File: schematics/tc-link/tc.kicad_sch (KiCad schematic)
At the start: 7 parts, among them U1 MAX31856

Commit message: Nearly completly schematics
Signed-off-by: Andrew Balmos <abalmos@purdue.edu>
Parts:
- renumbered C1 to C4, C3 to C5, C4 to C6, C5 to C7, R1 to R3, R2 to R4, U1 to U2
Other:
- moved on the sheet: C7
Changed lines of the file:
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@@
 	(wire
 		(pts
-			(xy 170.18 123.19) (xy 170.18 125.73)
+			(xy 218.44 72.39) (xy 218.44 74.93)
 		)
 		(stroke
@@
 	(wire
 		(pts
-			(xy 170.18 130.81) (xy 170.18 133.35)
+			(xy 218.44 80.01) (xy 218.44 82.55)
 		)
 		(stroke
@@
 	(symbol
 		(lib_id "power:+3V3")
-		(at 170.18 123.19 0)
+		(at 218.44 72.39 0)
 		(unit 1)
 		(exclude_from_sim no)
@@
 		(dnp no)
 		(fields_autoplaced yes)
-		(property "Reference" "#PWR013"
-			(at 170.18 127 0)
+		(property "Reference" "#PWR040"
+			(at 218.44 76.2 0)
 			(effects
 				(font
@@
 		)
 		(property "Value" "+3V3"
-			(at 170.18 118.11 0)
+			(at 218.44 67.31 0)
 			(effects
 				(font
@@
 		)
 		(property "Footprint" ""
-			(at 170.18 123.19 0)
+			(at 218.44 72.39 0)
 			(effects
 				(font
@@
 		)
 		(property "Datasheet" ""
-			(at 170.18 123.19 0)
+			(at 218.44 72.39 0)
 			(effects
 				(font
@@
 		)
 		(property "Description" "Power symbol creates a global label with name \"+3V3\""
-			(at 170.18 123.19 0)
+			(at 218.44 72.39 0)
 			(effects
 				(font
@@
 			(project "tc-link"
 				(path "/8e86abba-54e7-4e79-af31-15eabcc8dc53/cf0945b2-2b77-4b7a-9180-f6abb82eccbe"
-					(reference "#PWR010")
+					(reference "#PWR046")
 					(unit 1)
 				)
 				(path "/8e86abba-54e7-4e79-af31-15eabcc8dc53/d82a3210-8cdf-44cf-8f3c-363268ea9818"
-					(reference "#PWR013")
+					(reference "#PWR040")
 					(unit 1)
 				)
@@
 	(symbol
 		(lib_id "power:GND")
-		(at 170.18 133.35 0)
+		(at 218.44 82.55 0)
 		(unit 1)
 		(exclude_from_sim no)
@@
 		(dnp no)
 		(fields_autoplaced yes)
-		(property "Reference" "#PWR014"
-			(at 170.18 139.7 0)
+		(property "Reference" "#PWR041"
+			(at 218.44 88.9 0)
 			(effects
 				(font
@@
 		)
 		(property "Value" "GND"
-			(at 170.18 138.43 0)
+			(at 218.44 87.63 0)
 			(effects
 				(font
@@
 		)
 		(property "Footprint" ""
-			(at 170.18 133.35 0)
+			(at 218.44 82.55 0)
 			(effects
 				(font
@@
 		)
 		(property "Datasheet" ""
-			(at 170.18 133.35 0)
+			(at 218.44 82.55 0)
 			(effects
 				(font
@@
 		)
 		(property "Description" "Power symbol creates a global label with name \"GND\" , ground"
-			(at 170.18 133.35 0)
+			(at 218.44 82.55 0)
 			(effects
 				(font
@@
 			(project "tc-link"
 				(path "/8e86abba-54e7-4e79-af31-15eabcc8dc53/cf0945b2-2b77-4b7a-9180-f6abb82eccbe"
-					(reference "#PWR012")
+					(reference "#PWR047")
 					(unit 1)
 				)
 				(path "/8e86abba-54e7-4e79-af31-15eabcc8dc53/d82a3210-8cdf-44cf-8f3c-363268ea9818"
-					(reference "#PWR014")
+					(reference "#PWR041")
 					(unit 1)
 				)
@@
 		(dnp no)
 		(fields_autoplaced yes)
-		(property "Reference" "C3"
+		(property "Reference" "C5"
 			(at 134.62 76.1935 0)
 			(effects
@@
 			(project "tc-link"
 				(path "/8e86abba-54e7-4e79-af31-15eabcc8dc53/cf0945b2-2b77-4b7a-9180-f6abb82eccbe"
-					(reference "C12")
+					(reference "C9")
 					(unit 1)
 				)
 				(path "/8e86abba-54e7-4e79-af31-15eabcc8dc53/d82a3210-8cdf-44cf-8f3c-363268ea9818"
-					(reference "C3")
+					(reference "C5")
 					(unit 1)
 				)
@@
 		(dnp no)
 		(fields_autoplaced yes)
-		(property "Reference" "R1"
+		(property "Reference" "R3"
 			(at 123.19 66.04 90)
 			(effects
@@
 			(project "tc-link"
 				(path "/8e86abba-54e7-4e79-af31-15eabcc8dc53/cf0945b2-2b77-4b7a-9180-f6abb82eccbe"
-					(reference "R1")
+					(reference "R5")
 					(unit 1)
 				)
 				(path "/8e86abba-54e7-4e79-af31-15eabcc8dc53/d82a3210-8cdf-44cf-8f3c-363268ea9818"
-					(reference "R1")
+					(reference "R3")
 					(unit 1)
 				)
@@
 		(dnp no)
 		(fields_autoplaced yes)
-		(property "Reference" "C4"
+		(property "Reference" "C6"
 			(at 134.62 86.3535 0)
 			(effects
@@
 			(project "tc-link"
 				(path "/8e86abba-54e7-4e79-af31-15eabcc8dc53/cf0945b2-2b77-4b7a-9180-f6abb82eccbe"
-					(reference "C16")
+					(reference "C10")
 					(unit 1)
 				)
 				(path "/8e86abba-54e7-4e79-af31-15eabcc8dc53/d82a3210-8cdf-44cf-8f3c-363268ea9818"
-					(reference "C4")
+					(reference "C6")
 					(unit 1)
 				)
@@
 		(dnp no)
 		(fields_autoplaced yes)
-		(property "Reference" "C1"
+		(property "Reference" "C4"
 			(at 134.62 64.7635 0)
 			(effects
@@
 			(project "tc-link"
 				(path "/8e86abba-54e7-4e79-af31-15eabcc8dc53/cf0945b2-2b77-4b7a-9180-f6abb82eccbe"
-					(reference "C14")
+					(reference "C8")
 					(unit 1)
 				)
 				(path "/8e86abba-54e7-4e79-af31-15eabcc8dc53/d82a3210-8cdf-44cf-8f3c-363268ea9818"
-					(reference "C1")
+					(reference "C4")
 					(unit 1)
 				)
@@
 		(dnp no)
 		(fields_autoplaced yes)
-		(property "Reference" "R2"
+		(property "Reference" "R4"
 			(at 123.19 76.2 90)
 			(effects
@@
 			(project "tc-link"
 				(path "/8e86abba-54e7-4e79-af31-15eabcc8dc53/cf0945b2-2b77-4b7a-9180-f6abb82eccbe"
-					(reference "R8")
+					(reference "R6")
 					(unit 1)
 				)
 				(path "/8e86abba-54e7-4e79-af31-15eabcc8dc53/d82a3210-8cdf-44cf-8f3c-363268ea9818"
-					(reference "R2")
+					(reference "R4")
 					(unit 1)
 				)
@@
 		(dnp no)
 		(fields_autoplaced yes)
-		(property "Reference" "#PWR05"
+		(property "Reference" "#PWR036"
 			(at 128.27 64.77 0)
 			(effects
@@
 			(project "tc-link"
 				(path "/8e86abba-54e7-4e79-af31-15eabcc8dc53/cf0945b2-2b77-4b7a-9180-f6abb82eccbe"
-					(reference "#PWR032")
+					(reference "#PWR042")
 					(unit 1)
 				)
 				(path "/8e86abba-54e7-4e79-af31-15eabcc8dc53/d82a3210-8cdf-44cf-8f3c-363268ea9818"
-					(reference "#PWR05")
+					(reference "#PWR036")
 					(unit 1)
 				)
@@
 		(dnp no)
 		(fields_autoplaced yes)
-		(property "Reference" "U1"
+		(property "Reference" "U2"
 			(at 172.3233 60.96 0)
 			(effects
@@
 			(project "tc-link"
 				(path "/8e86abba-54e7-4e79-af31-15eabcc8dc53/cf0945b2-2b77-4b7a-9180-f6abb82eccbe"
-					(reference "U1")
+					(reference "U3")
 					(unit 1)
 				)
 				(path "/8e86abba-54e7-4e79-af31-15eabcc8dc53/d82a3210-8cdf-44cf-8f3c-363268ea9818"
-					(reference "U1")
+					(reference "U2")
 					(unit 1)
 				)
@@
 	(symbol
 		(lib_id "Device:C_Small")
-		(at 170.18 128.27 0)
+		(at 218.44 77.47 0)
 		(unit 1)
 		(exclude_from_sim no)
@@
 		(dnp no)
 		(fields_autoplaced yes)
-		(property "Reference" "C5"
-			(at 172.72 127.0062 0)
+		(property "Reference" "C7"
+			(at 220.98 76.2062 0)
 			(effects
 				(font
@@
 		)
 		(property "Value" "100n"
-			(at 172.72 129.5462 0)
+			(at 220.98 78.7462 0)
 			(effects
 				(font
@@
 		)
 		(property "Footprint" ""
-			(at 170.18 128.27 0)
+			(at 218.44 77.47 0)
 			(effects
 				(font
@@
 		)
 		(property "Datasheet" "~"
-			(at 170.18 128.27 0)
+			(at 218.44 77.47 0)
 			(effects
 				(font
@@
 		)
 		(property "Description" "Unpolarized capacitor, small symbol"
-			(at 170.18 128.27 0)
+			(at 218.44 77.47 0)
 			(effects
 				(font
@@
 			(project "tc-link"
 				(path "/8e86abba-54e7-4e79-af31-15eabcc8dc53/cf0945b2-2b77-4b7a-9180-f6abb82eccbe"
-					(reference "C5")
+					(reference "C11")
 					(unit 1)
 				)
 				(path "/8e86abba-54e7-4e79-af31-15eabcc8dc53/d82a3210-8cdf-44cf-8f3c-363268ea9818"
-					(reference "C5")
+					(reference "C7")
 					(unit 1)
 				)
@@
 		(dnp no)
 		(fields_autoplaced yes)
-		(property "Reference" "#PWR07"
+		(property "Reference" "#PWR037"
 			(at 132.08 100.33 0)
 			(effects
@@
 			(project "tc-link"
 				(path "/8e86abba-54e7-4e79-af31-15eabcc8dc53/cf0945b2-2b77-4b7a-9180-f6abb82eccbe"
-					(reference "#PWR030")
+					(reference "#PWR043")
 					(unit 1)
 				)
 				(path "/8e86abba-54e7-4e79-af31-15eabcc8dc53/d82a3210-8cdf-44cf-8f3c-363268ea9818"
-					(reference "#PWR07")
+					(reference "#PWR037")
 					(unit 1)
 				)
@@
 		(dnp no)
 		(fields_autoplaced yes)
-		(property "Reference" "#PWR011"
+		(property "Reference" "#PWR039"
 			(at 167.64 104.14 0)
 			(effects
@@
 			(project "tc-link"
 				(path "/8e86abba-54e7-4e79-af31-15eabcc8dc53/cf0945b2-2b77-4b7a-9180-f6abb82eccbe"
-					(reference "#PWR06")
+					(reference "#PWR045")
 					(unit 1)
 				)
 				(path "/8e86abba-54e7-4e79-af31-15eabcc8dc53/d82a3210-8cdf-44cf-8f3c-363268ea9818"
-					(reference "#PWR011")
+					(reference "#PWR039")
 					(unit 1)
 				)
@@
 		(dnp no)
 		(fields_autoplaced yes)
-		(property "Reference" "#PWR09"
+		(property "Reference" "#PWR038"
 			(at 167.64 59.69 0)
 			(effects
@@
 			(project "tc-link"
 				(path "/8e86abba-54e7-4e79-af31-15eabcc8dc53/cf0945b2-2b77-4b7a-9180-f6abb82eccbe"
-					(reference "#PWR08")
+					(reference "#PWR044")
 					(unit 1)
 				)
 				(path "/8e86abba-54e7-4e79-af31-15eabcc8dc53/d82a3210-8cdf-44cf-8f3c-363268ea9818"
-					(reference "#PWR09")
-					(unit 1)
-				)
+					(reference "#PWR038")
+					(unit 1)
+				)

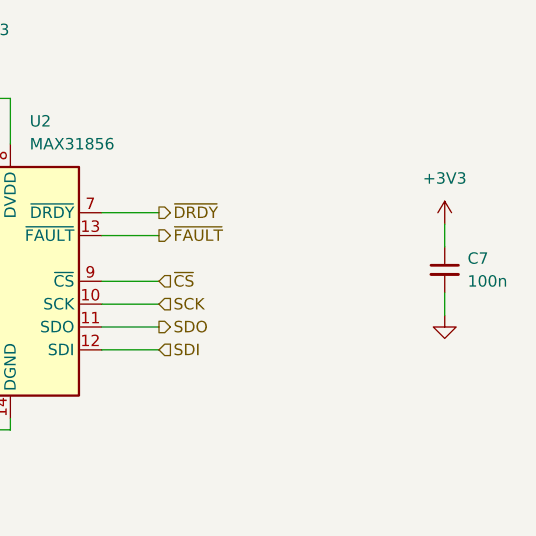
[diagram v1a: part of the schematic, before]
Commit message: release(tc-link): v1.0. Sent for production.
Signed-off-by: Andrew Balmos <abalmos@purdue.edu>
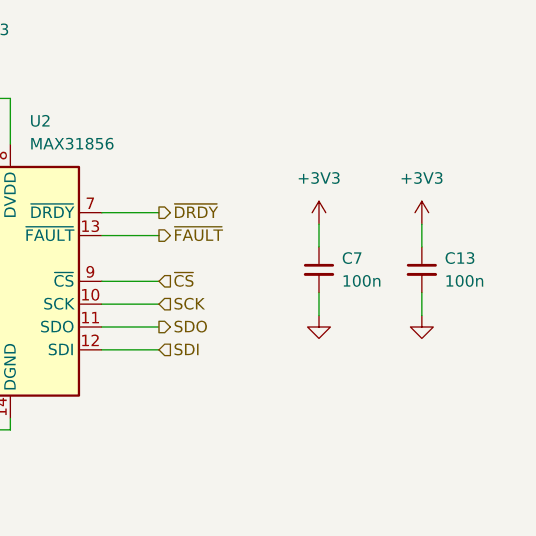
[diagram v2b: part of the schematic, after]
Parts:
- added C13: 100n, Capacitor_SMD:C_0603_1608Metric, symbol Device:C_Small
- C4, C6: footprint Capacitor_SMD:C_0402_1005Metric -> Capacitor_SMD:C_0603_1608Metric; LCSC (none) -> C327204; MPN (none) -> CC0603KRX7R8BB103
- C5: footprint Capacitor_SMD:C_0402_1005Metric -> Capacitor_SMD:C_0603_1608Metric; LCSC (none) -> C6119867; MPN (none) -> CGA0603X7R104K500JT
- C7: footprint (none) -> Capacitor_SMD:C_0603_1608Metric; LCSC (none) -> C6119867; MPN (none) -> CGA0603X7R104K500JT
- R3, R4: footprint (none) -> Resistor_SMD:R_0603_1608Metric; LCSC (none) -> C22356621; MPN (none) -> RCA03100RJLF
- U2: symbol Sensor_Temperature:MAX31856 -> Link_Components:MAX31856; LCSC (none) -> C2653162; MPN (none) -> MAX31856MUD+T
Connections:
- net +3V3: now also C13.1
- net GND: now also C13.2
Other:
- moved on the sheet: C7
